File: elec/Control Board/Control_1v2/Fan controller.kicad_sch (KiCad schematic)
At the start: 37 parts, among them J10 Conn_01x05, J11 Conn_01x04, J12 Conn_01x07, J20 Conn_01x04, J6 DB25_Female_MountingHoles, J9 Conn_01x04, Q2 NCE01P30K, Q601 BSS138

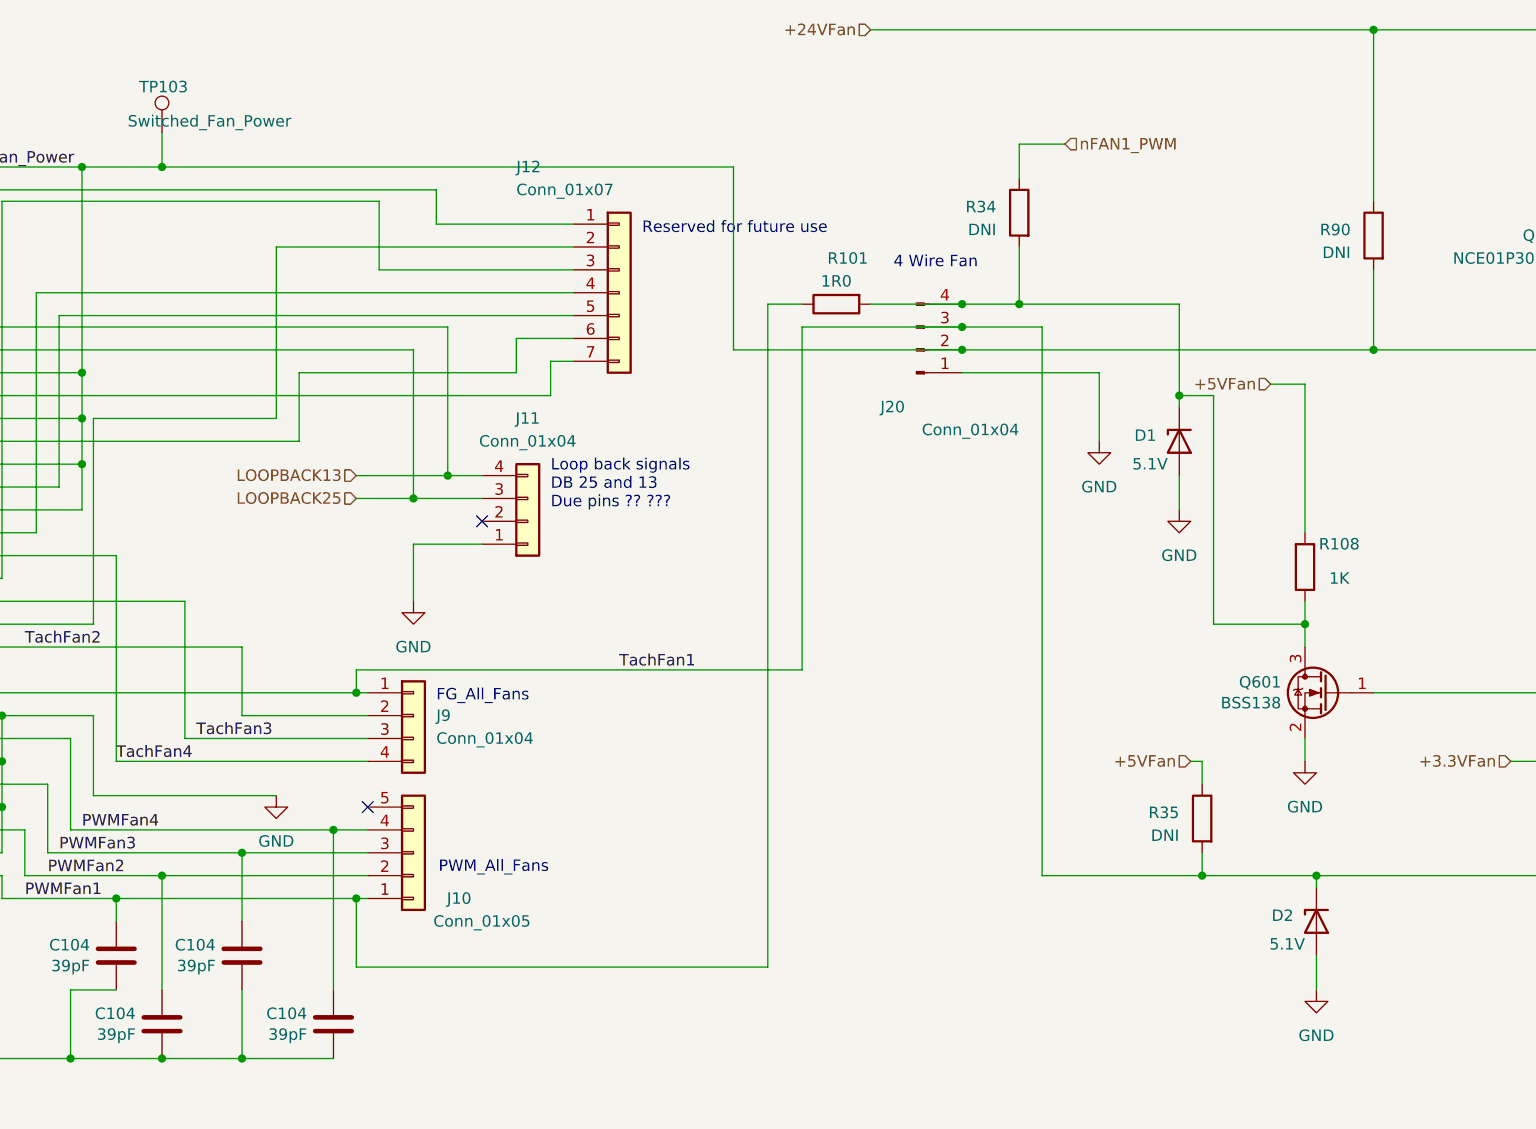
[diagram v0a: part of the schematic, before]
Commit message: Contrl 1.2 schematic, fix for Issue: Tach Failure, Missplugged at J20, Update J20 with Key #166
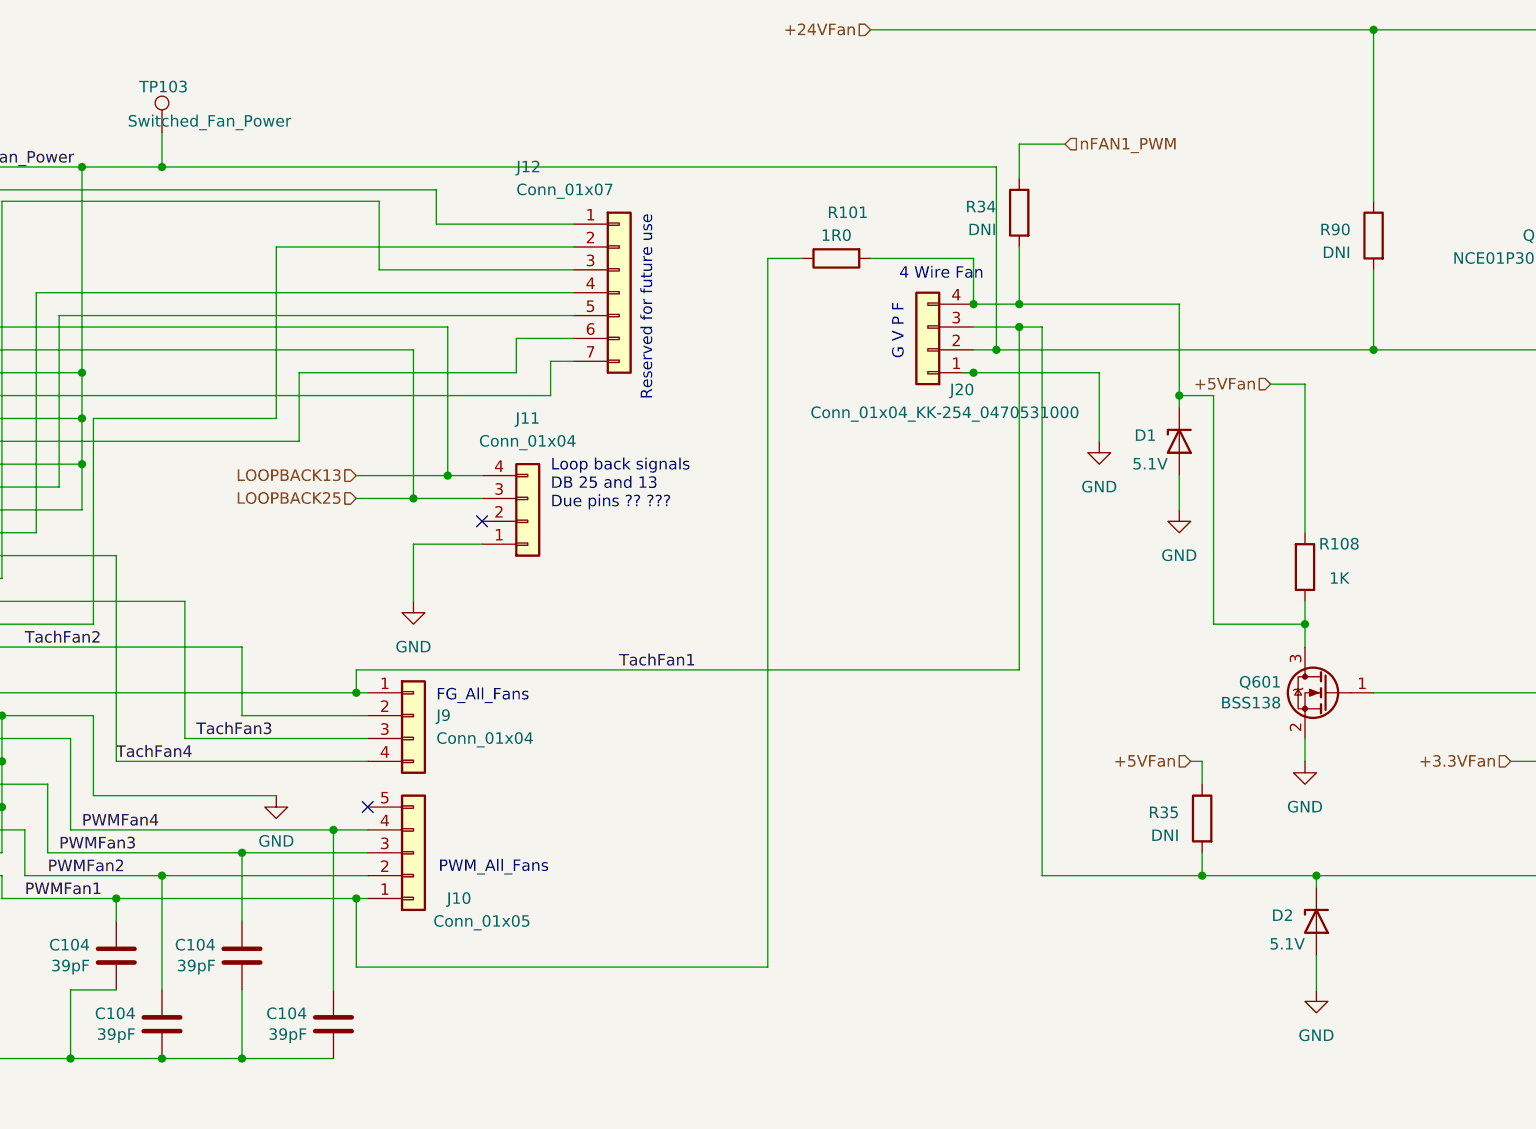
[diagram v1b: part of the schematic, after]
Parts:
- removed J20: Conn_01x04, Connector_PinHeader_2.54mm:PinHeader_1x04_P2.54mm_Vertical, symbol Connector:Conn_01x04_Pin
- added J20: Conn_01x04_KK-254_0470531000, PubInv_KiCad_PCB:Molex_KK-254_0470531000_1x04_P2.54mm_Vertical_ForFAN, symbol Connector_Generic:Conn_01x04
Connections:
- net GND: now also J20.1 (Pin_1)
- net Switched_Fan_Power: now also J20.2 (Pin_2)
- net TachFan1: now also J20.3 (Pin_3)
- net at D1.1 (K), Q601.3 (D), R101.2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: now also J20.4 (Pin_4)
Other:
- note added: "G V P F"
- moved on the sheet: R101

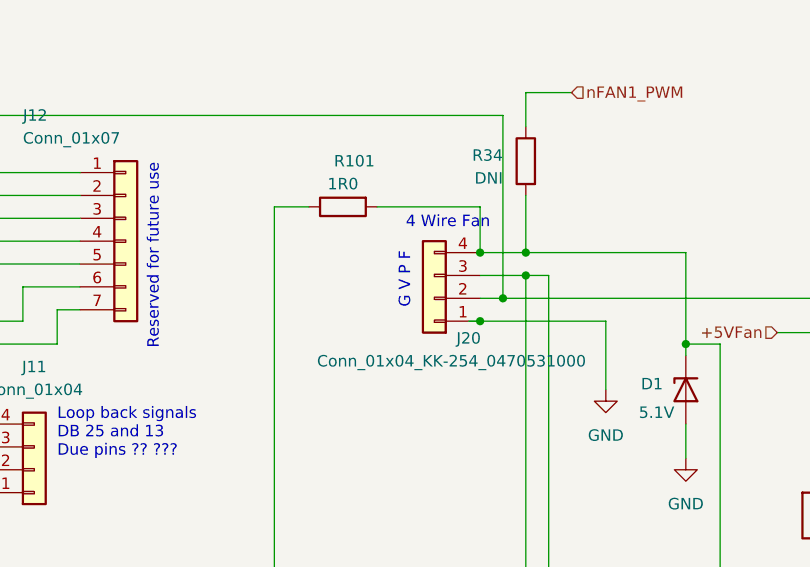
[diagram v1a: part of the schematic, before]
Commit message: Contrl 1.2 PCB, fix for Issue: Fan connector routing.
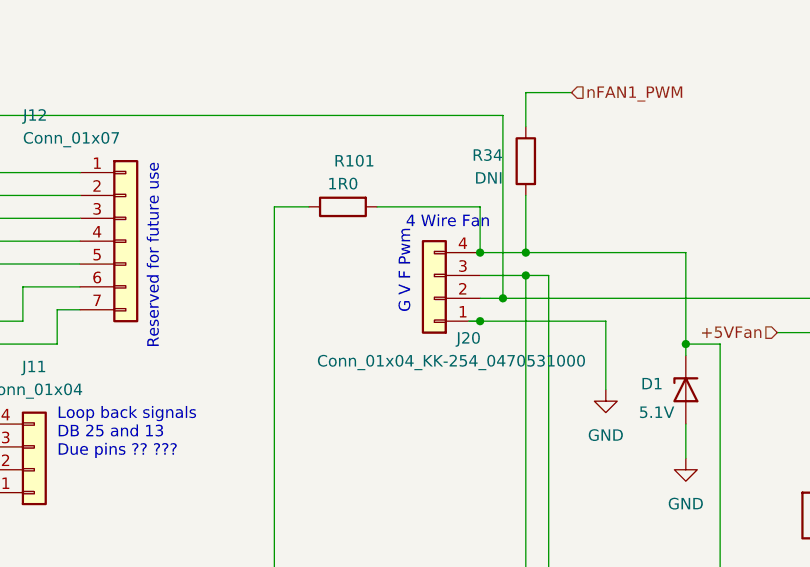
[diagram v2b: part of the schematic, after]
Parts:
- J20: Cost (none) -> 0.1404; Distributor 1 (none) -> Digikey; Distributor 1 PN (none) -> WM4330-ND; Distributor 2 (none) -> JLCPCB; Distributor 2 PN (none) -> C3025061; MPN (none) -> 0470531000; Manufacturer (none) -> Molex
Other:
- note added: "G V F Pwm"
- note removed: "G V P F"
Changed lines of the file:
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@@
     (effects (font (size 1.27 1.27)) (justify left bottom))
   )
-  (text "G V P F" (at 219.71 76.2 90)
+  (text "G V F Pwm" (at 219.71 73.66 90)
     (effects (font (size 1.27 1.27)) (justify right bottom))
   )
@@
       (effects (font (size 1.27 1.27)) hide)
     )
-    (property "Datasheet" "~" (at 222.25 81.28 0)
-      (effects (font (size 1.27 1.27)) hide)
-    )
+    (property "Datasheet" "470531000_sd.pdf" (at 222.25 81.28 0)
+      (effects (font (size 1.27 1.27)) hide)
+    )
+    (property "Cost" "0.1404" (at 222.25 81.28 0)
+      (effects (font (size 1.27 1.27)) hide)
+    )
+    (property "Description" "Plugin,P=2.54mm Pin Headers ROHS FAN" (at 222.25 81.28 0)
+      (effects (font (size 1.27 1.27)) hide)
+    )
+    (property "Distributor 1" "Digikey" (at 222.25 81.28 0)
+      (effects (font (size 1.27 1.27)) hide)
+    )
+    (property "Distributor 1 PN" "WM4330-ND" (at 222.25 81.28 0)
+      (effects (font (size 1.27 1.27)) hide)
+    )
+    (property "Distributor 2" "JLCPCB" (at 222.25 81.28 0)
+      (effects (font (size 1.27 1.27)) hide)
+    )
+    (property "Distributor 2 PN" "C3025061" (at 222.25 81.28 0)
+      (effects (font (size 1.27 1.27)) hide)
+    )
+    (property "MPN" "0470531000" (at 222.25 81.28 0)
+      (effects (font (size 1.27 1.27)) hide)
+    )
+    (property "Manufacturer" "Molex" (at 222.25 81.28 0)
+      (effects (font (size 1.27 1.27)) hide)
+    )

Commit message: Contrl 1.2 schematic, fix incorrect signal nameing on J20.
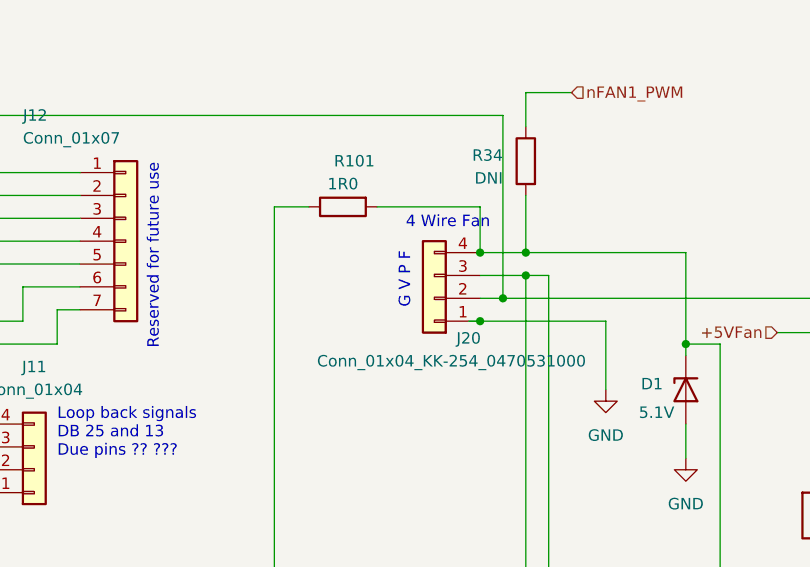
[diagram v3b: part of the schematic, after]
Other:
- note added: "G V P F"
- note removed: "G V F Pwm"
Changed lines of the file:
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@@
     (effects (font (size 1.27 1.27)) (justify left bottom))
   )
-  (text "G V F Pwm" (at 219.71 73.66 90)
+  (text "G V P F" (at 219.71 76.2 90)
     (effects (font (size 1.27 1.27)) (justify right bottom))
   )

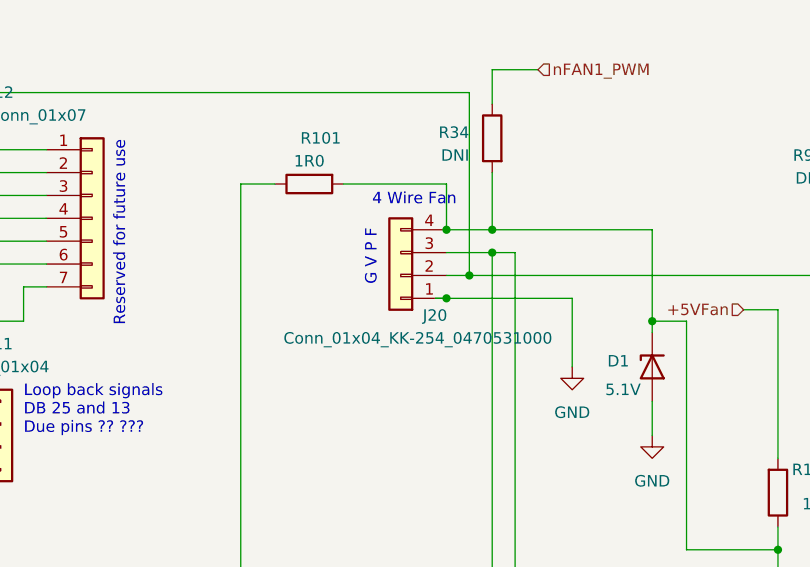
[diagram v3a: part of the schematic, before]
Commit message: Contrl 1.2 schematic, fix incorrect signal nameing on J20.
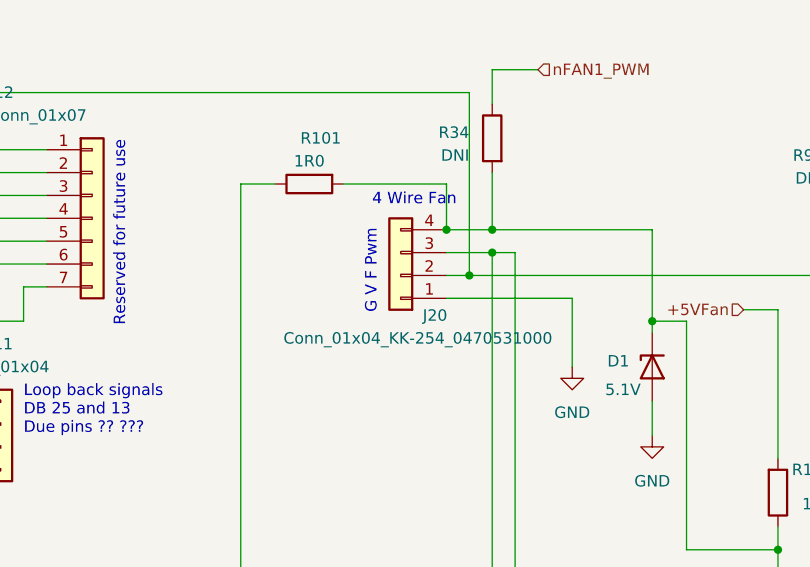
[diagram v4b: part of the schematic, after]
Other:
- note added: "G V F Pwm"
- note removed: "G V P F"
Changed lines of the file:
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@@
   (junction (at 132.08 142.24) (diameter 0) (color 0 0 0 0)
   )
-  (junction (at 227.33 83.82) (diameter 0) (color 0 0 0 0)
-  )
   (junction (at 119.38 132.08) (diameter 0) (color 0 0 0 0)
   )
@@
     (stroke (width 0) (type default))
   )
-  (wire (pts (xy 226.06 83.82) (xy 227.33 83.82))
-    (stroke (width 0) (type default))
-  )
   (wire (pts (xy 104.14 101.6) (xy 123.19 101.6))
     (stroke (width 0) (type default))
@@
     (effects (font (size 1.27 1.27)) (justify left bottom))
   )
-  (text "G V P F" (at 219.71 76.2 90)
+  (text "G V F Pwm" (at 219.71 76.2 90)
     (effects (font (size 1.27 1.27)) (justify right bottom))
   )

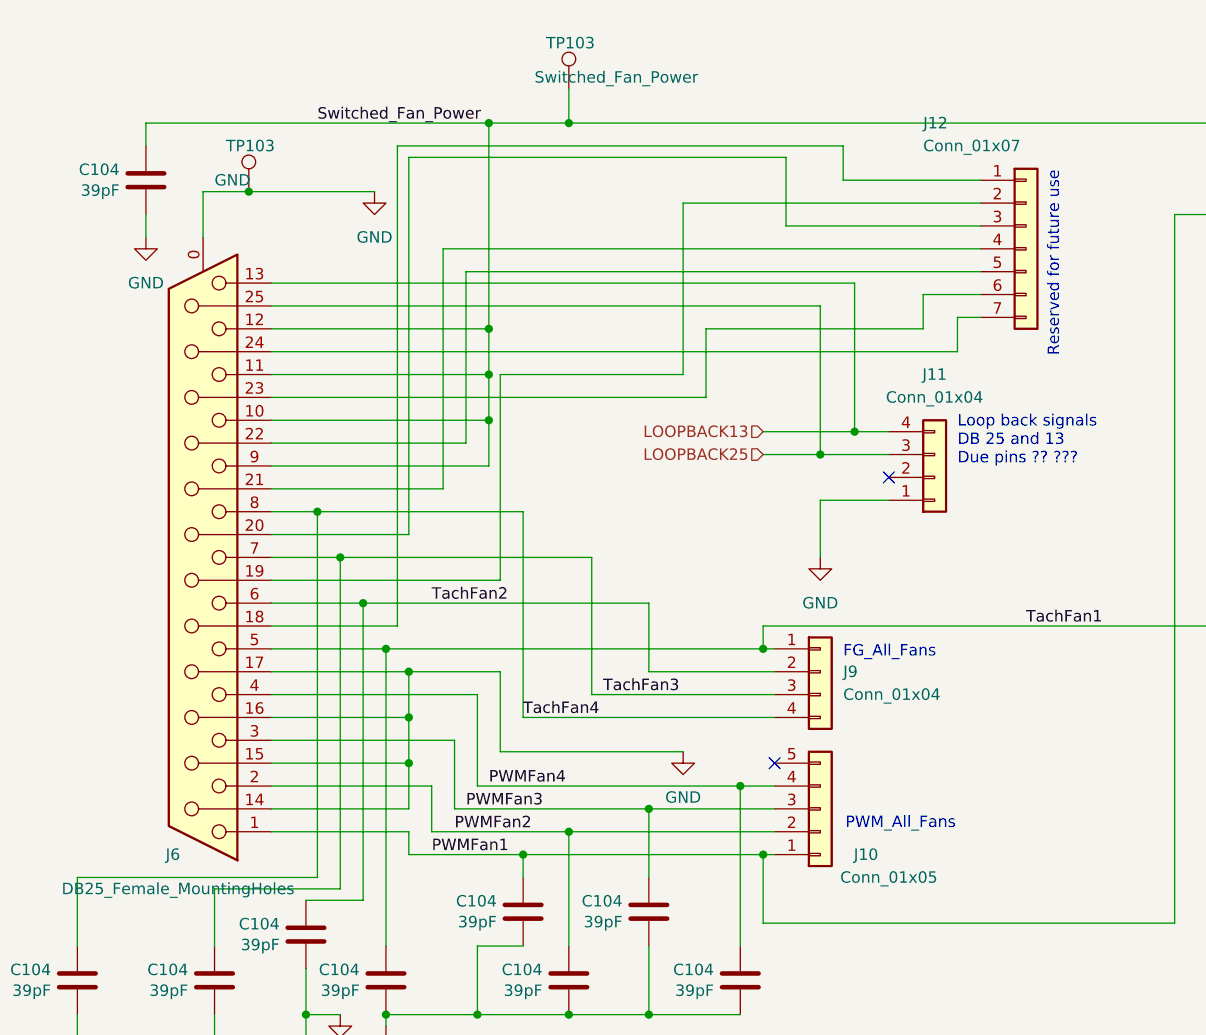
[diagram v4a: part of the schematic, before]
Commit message: PCB V1.2. Add 3d model for power supply footprint. Set many headers connectors for DNI on schematic and PCB.
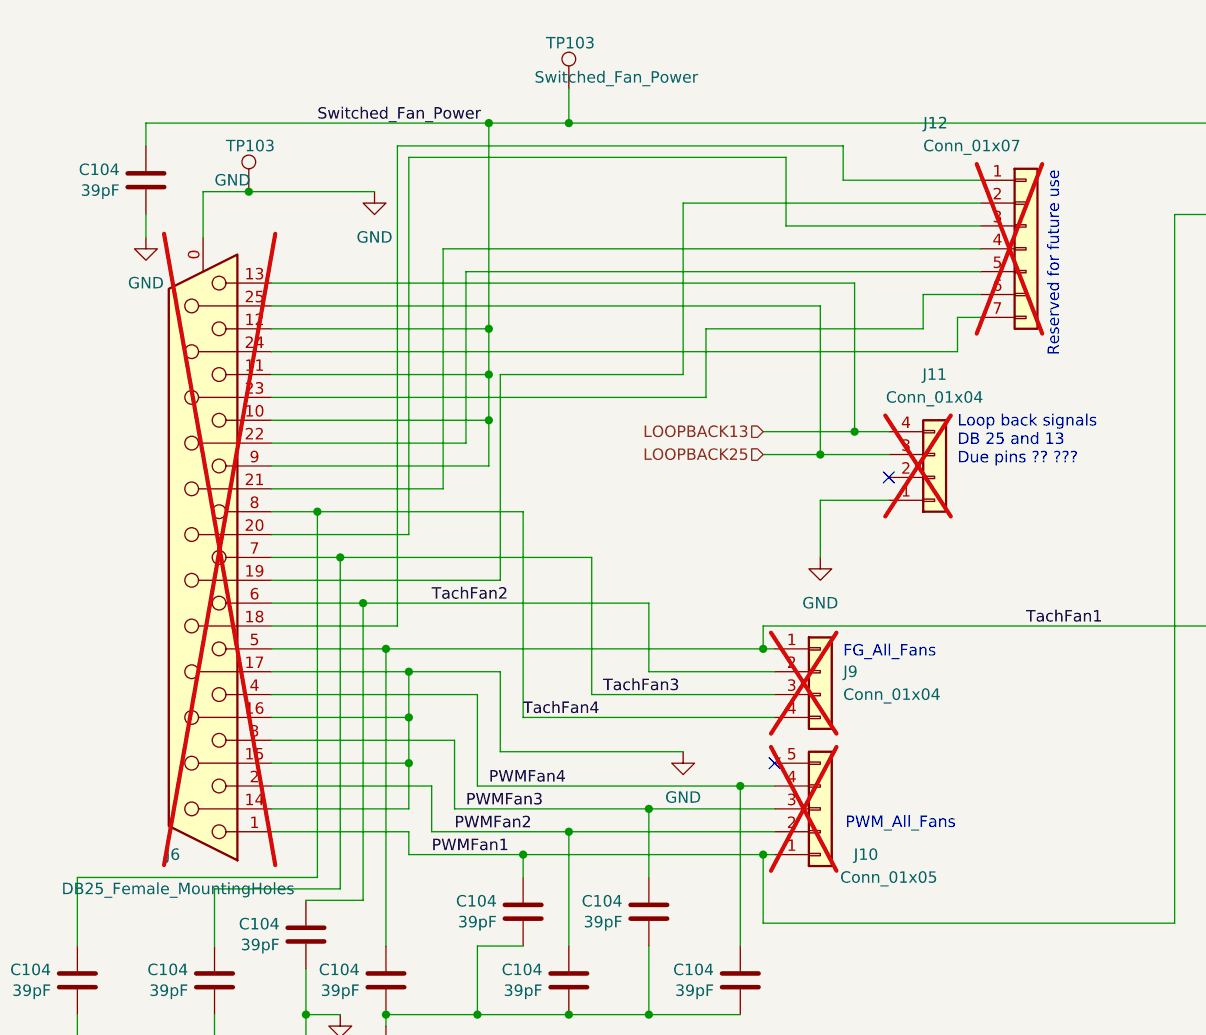
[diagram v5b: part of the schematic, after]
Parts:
- J10, J11, J12, J6, J9: now not fitted; now left out of the parts list
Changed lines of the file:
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@@
   )
   (symbol (lib_id "Connector_Generic:Conn_01x04") (at 165.1 121.92 0) (unit 1)
-    (in_bom yes) (on_board yes) (dnp no) (fields_autoplaced)
+    (in_bom no) (on_board yes) (dnp yes) (fields_autoplaced)
     (property "Reference" "J9" (at 167.64 121.9199 0)
       (effects (font (size 1.27 1.27)) (justify left))
@@
   )
   (symbol (lib_id "Connector_Generic:Conn_01x04") (at 177.8 100.33 0) (mirror x) (unit 1)
-    (in_bom yes) (on_board yes) (dnp no) (fields_autoplaced)
+    (in_bom no) (on_board yes) (dnp yes) (fields_autoplaced)
     (property "Reference" "J11" (at 177.8 88.9 0)
       (effects (font (size 1.27 1.27)))
@@
   )
   (symbol (lib_id "Connector_Generic:Conn_01x05") (at 165.1 137.16 0) (mirror x) (unit 1)
-    (in_bom yes) (on_board yes) (dnp no)
+    (in_bom no) (on_board yes) (dnp yes)
     (property "Reference" "J10" (at 170.18 142.24 0)
       (effects (font (size 1.27 1.27)))
@@
   )
   (symbol (lib_id "Connector:DB25_Female_MountingHoles") (at 96.52 109.22 180) (unit 1)
-    (in_bom yes) (on_board yes) (dnp no)
+    (in_bom no) (on_board yes) (dnp yes)
     (property "Reference" "J6" (at 93.98 142.24 0)
       (effects (font (size 1.27 1.27)) (justify left))
@@
   )
   (symbol (lib_id "Connector_Generic:Conn_01x07") (at 187.96 74.93 0) (unit 1)
-    (in_bom yes) (on_board yes) (dnp no)
+    (in_bom no) (on_board yes) (dnp yes)
     (property "Reference" "J12" (at 176.53 60.96 0)
       (effects (font (size 1.27 1.27)) (justify left))
